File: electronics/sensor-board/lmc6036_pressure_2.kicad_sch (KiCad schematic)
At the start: 10 parts, among them U13 LMC6036, U17 LMC6036

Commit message: work on sensor-board
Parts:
- removed U13, U17: LMC6036, LMC6036:SOP65P640X120-14N, symbol LMC6036_custom:LMC6036
- added U12: LMC6036, LMC6036:SOP65P640X120-14N, symbol LMC6036_custom:LMC6036
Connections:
- net VDD: now also U12.4 (VDD)
- net VSS: now also U12.11 (VSS)
- net output_A: now also U12.1 (OUTA), U12.2 (INA-)
- net output_B: now also U12.6 (INB-), U12.7 (OUTB)
- net output_C: now also U12.8 (OUTC), U12.9 (INC-)
- net output_D: now also U12.13 (IND-), U12.14 (OUTD)
- net at R92.1, R96.1: now also U12.10 (INC+)
- net at R90.1, R94.1: now also U12.3 (INA+)
- net at R93.1, R97.1: now also U12.12 (IND+)
- net at R91.1, R95.1: now also U12.5 (INB+)
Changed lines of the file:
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@@
   (junction (at 142.24 120.65) (diameter 0) (color 0 0 0 0))
   (junction (at 142.24 148.59) (diameter 0) (color 0 0 0 0))
-  (junction (at 162.56 63.5) (diameter 0) (color 0 0 0 0))
-  (junction (at 162.56 90.17) (diameter 0) (color 0 0 0 0))
-  (junction (at 162.56 118.11) (diameter 0) (color 0 0 0 0))
-  (junction (at 162.56 146.05) (diameter 0) (color 0 0 0 0))
   (wire (pts (xy 125.73 60.96) (xy 135.89 60.96))
     (stroke (width 0) (type default) (color 0 0 0 0))
@@
   (symbol (lib_id "LMC6036_custom:LMC6036") (at 153.67 44.45 90) (unit 5)
     (in_bom yes) (on_board yes) (fields_autoplaced)
-    (property "Reference" "U13" (id 0) (at 153.67 35.56 90))
+    (property "Reference" "U12" (id 0) (at 153.67 35.56 90))
     (property "Value" "LMC6036" (id 1) (at 153.67 38.1 90))
     (property "Footprint" "LMC6036:SOP65P640X120-14N" (id 2) (at 153.67 42.545 0)
@@
   )
   (symbol (lib_id "LMC6036_custom:LMC6036") (at 153.67 63.5 0) (unit 1)
-    (in_bom yes) (on_board yes)
-    (property "Reference" "U17" (id 0) (at 154.94 53.34 0))
-    (property "Value" "LMC6036" (id 1) (at 160.02 68.58 0))
+    (in_bom yes) (on_board yes) (fields_autoplaced)
+    (property "Reference" "U12" (id 0) (at 154.94 53.34 0))
+    (property "Value" "LMC6036" (id 1) (at 154.94 55.88 0))
     (property "Footprint" "LMC6036:SOP65P640X120-14N" (id 2) (at 155.575 63.5 0)
       (effects (font (size 1.27 1.27)) hide)
@@
   (symbol (lib_id "LMC6036_custom:LMC6036") (at 153.67 90.17 0) (unit 2)
     (in_bom yes) (on_board yes) (fields_autoplaced)
-    (property "Reference" "U13" (id 0) (at 154.94 80.01 0))
+    (property "Reference" "U12" (id 0) (at 154.94 80.01 0))
     (property "Value" "LMC6036" (id 1) (at 154.94 82.55 0))
     (property "Footprint" "LMC6036:SOP65P640X120-14N" (id 2) (at 155.575 90.17 0)
@@
   (symbol (lib_id "LMC6036_custom:LMC6036") (at 153.67 118.11 0) (unit 3)
     (in_bom yes) (on_board yes) (fields_autoplaced)
-    (property "Reference" "U13" (id 0) (at 154.94 107.95 0))
+    (property "Reference" "U12" (id 0) (at 154.94 107.95 0))
     (property "Value" "LMC6036" (id 1) (at 154.94 110.49 0))
     (property "Footprint" "LMC6036:SOP65P640X120-14N" (id 2) (at 155.575 118.11 0)
@@
   (symbol (lib_id "LMC6036_custom:LMC6036") (at 153.67 146.05 0) (unit 4)
     (in_bom yes) (on_board yes) (fields_autoplaced)
-    (property "Reference" "U13" (id 0) (at 154.94 135.89 0))
+    (property "Reference" "U12" (id 0) (at 154.94 135.89 0))
     (property "Value" "LMC6036" (id 1) (at 154.94 138.43 0))
     (property "Footprint" "LMC6036:SOP65P640X120-14N" (id 2) (at 155.575 146.05 0)

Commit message: More work on sensor-board
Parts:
- R90, R91, R92, R93, R94, R95, R96, R97: value 150 -> 100
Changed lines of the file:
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@@
     (in_bom yes) (on_board yes) (fields_autoplaced)
     (property "Reference" "R92" (id 0) (at 135.89 114.3 90))
-    (property "Value" "150" (id 1) (at 135.89 116.84 90))
+    (property "Value" "100" (id 1) (at 135.89 116.84 90))
     (property "Footprint" "Resistor_SMD:R_0603_1608Metric" (id 2) (at 135.89 118.872 90)
       (effects (font (size 1.27 1.27)) hide)
@@
     (in_bom yes) (on_board yes) (fields_autoplaced)
     (property "Reference" "R93" (id 0) (at 135.89 142.24 90))
-    (property "Value" "150" (id 1) (at 135.89 144.78 90))
+    (property "Value" "100" (id 1) (at 135.89 144.78 90))
     (property "Footprint" "Resistor_SMD:R_0603_1608Metric" (id 2) (at 135.89 146.812 90)
       (effects (font (size 1.27 1.27)) hide)
@@
     (in_bom yes) (on_board yes) (fields_autoplaced)
     (property "Reference" "R90" (id 0) (at 135.89 59.69 90))
-    (property "Value" "150" (id 1) (at 135.89 62.23 90))
+    (property "Value" "100" (id 1) (at 135.89 62.23 90))
     (property "Footprint" "Resistor_SMD:R_0603_1608Metric" (id 2) (at 135.89 64.262 90)
       (effects (font (size 1.27 1.27)) hide)
@@
       (effects (font (size 1.27 1.27)) (justify left))
     )
-    (property "Value" "150" (id 1) (at 144.78 72.3899 0)
+    (property "Value" "100" (id 1) (at 144.78 72.3899 0)
       (effects (font (size 1.27 1.27)) (justify left))
     )
@@
       (effects (font (size 1.27 1.27)) (justify left))
     )
-    (property "Value" "150" (id 1) (at 144.78 99.0599 0)
+    (property "Value" "100" (id 1) (at 144.78 99.0599 0)
       (effects (font (size 1.27 1.27)) (justify left))
     )
@@
     (in_bom yes) (on_board yes) (fields_autoplaced)
     (property "Reference" "R91" (id 0) (at 135.89 86.36 90))
-    (property "Value" "150" (id 1) (at 135.89 88.9 90))
+    (property "Value" "100" (id 1) (at 135.89 88.9 90))
     (property "Footprint" "Resistor_SMD:R_0603_1608Metric" (id 2) (at 135.89 90.932 90)
       (effects (font (size 1.27 1.27)) hide)
@@
       (effects (font (size 1.27 1.27)) (justify left))
     )
-    (property "Value" "150" (id 1) (at 144.78 154.9399 0)
+    (property "Value" "100" (id 1) (at 144.78 154.9399 0)
       (effects (font (size 1.27 1.27)) (justify left))
     )
@@
       (effects (font (size 1.27 1.27)) (justify left))
     )
-    (property "Value" "150" (id 1) (at 144.78 126.9999 0)
-      (effects (font (size 1.27 1.27)) (justify left))
-    )
+    (property "Value" "100" (id 1) (at 144.78 126.9999 0)
+      (effects (font (size 1.27 1.27)) (justify left))
+    )

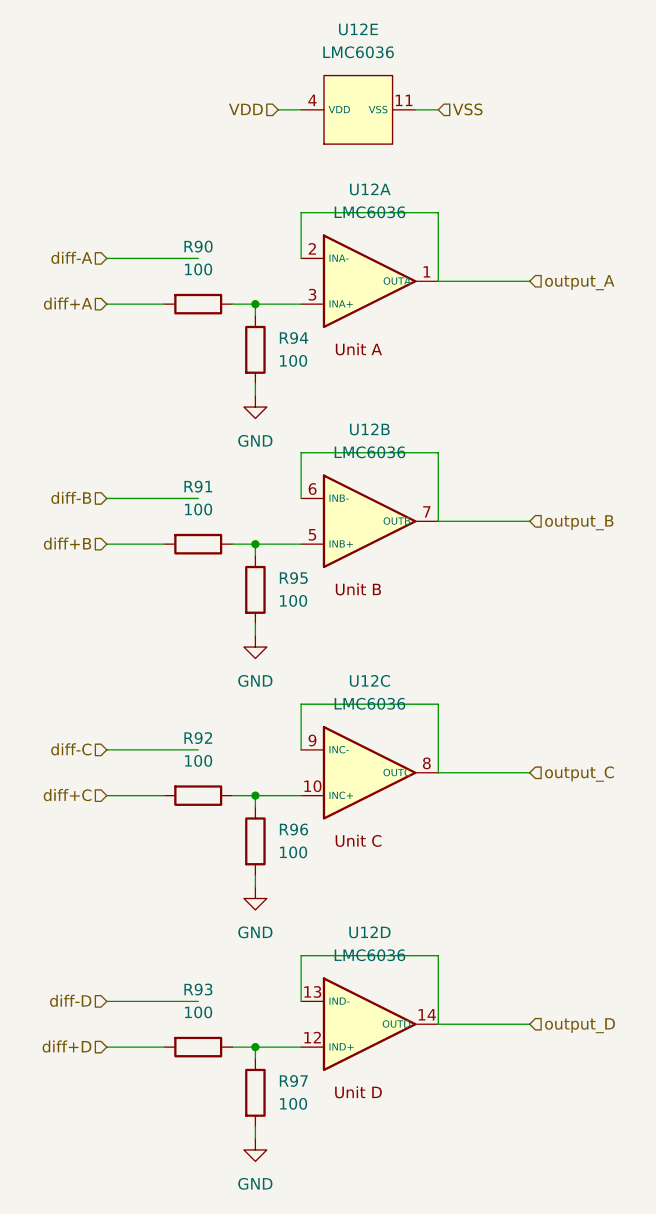
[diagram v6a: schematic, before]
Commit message: updated loadcell amplifier
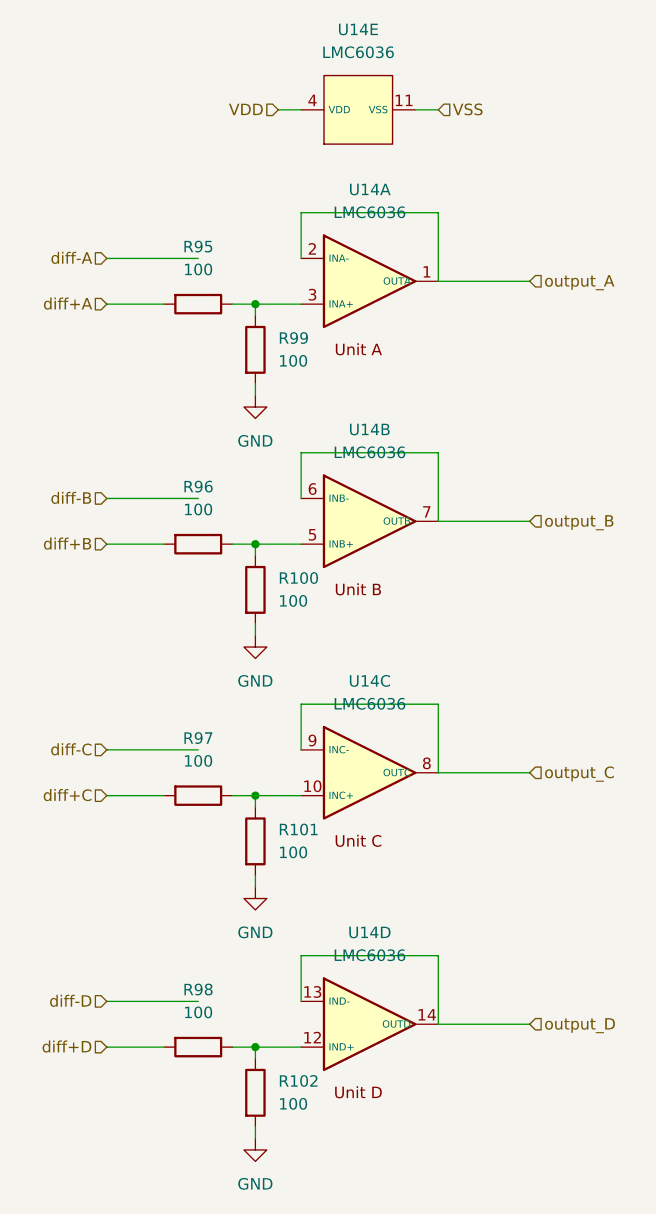
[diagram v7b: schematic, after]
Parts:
- renumbered R95 to R100, R96 to R101, R97 to R102, R90 to R95, R91 to R96, R92 to R97, R93 to R98, R94 to R99, U12 to U14
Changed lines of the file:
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@@
   (symbol (lib_id "Device:R") (at 135.89 120.65 270) (unit 1)
     (in_bom yes) (on_board yes) (fields_autoplaced)
-    (property "Reference" "R92" (id 0) (at 135.89 114.3 90))
+    (property "Reference" "R97" (id 0) (at 135.89 114.3 90))
     (property "Value" "100" (id 1) (at 135.89 116.84 90))
     (property "Footprint" "Resistor_SMD:R_0603_1608Metric" (id 2) (at 135.89 118.872 90)
@@
   (symbol (lib_id "power:GND") (at 142.24 102.87 0) (unit 1)
     (in_bom yes) (on_board yes) (fields_autoplaced)
-    (property "Reference" "#PWR0128" (id 0) (at 142.24 109.22 0)
+    (property "Reference" "#PWR0143" (id 0) (at 142.24 109.22 0)
       (effects (font (size 1.27 1.27)) hide)
     )
@@
   (symbol (lib_id "LMC6036_custom:LMC6036") (at 153.67 63.5 0) (unit 1)
     (in_bom yes) (on_board yes) (fields_autoplaced)
-    (property "Reference" "U12" (id 0) (at 154.94 53.34 0))
+    (property "Reference" "U14" (id 0) (at 154.94 53.34 0))
     (property "Value" "LMC6036" (id 1) (at 154.94 55.88 0))
     (property "Footprint" "LMC6036:SOP65P640X120-14N" (id 2) (at 155.575 63.5 0)
@@
   (symbol (lib_id "LMC6036_custom:LMC6036") (at 153.67 118.11 0) (unit 3)
     (in_bom yes) (on_board yes) (fields_autoplaced)
-    (property "Reference" "U12" (id 0) (at 154.94 107.95 0))
+    (property "Reference" "U14" (id 0) (at 154.94 107.95 0))
     (property "Value" "LMC6036" (id 1) (at 154.94 110.49 0))
     (property "Footprint" "LMC6036:SOP65P640X120-14N" (id 2) (at 155.575 118.11 0)
@@
   (symbol (lib_id "Device:R") (at 135.89 148.59 270) (unit 1)
     (in_bom yes) (on_board yes) (fields_autoplaced)
-    (property "Reference" "R93" (id 0) (at 135.89 142.24 90))
+    (property "Reference" "R98" (id 0) (at 135.89 142.24 90))
     (property "Value" "100" (id 1) (at 135.89 144.78 90))
     (property "Footprint" "Resistor_SMD:R_0603_1608Metric" (id 2) (at 135.89 146.812 90)
@@
   (symbol (lib_id "Device:R") (at 135.89 66.04 270) (unit 1)
     (in_bom yes) (on_board yes) (fields_autoplaced)
-    (property "Reference" "R90" (id 0) (at 135.89 59.69 90))
+    (property "Reference" "R95" (id 0) (at 135.89 59.69 90))
     (property "Value" "100" (id 1) (at 135.89 62.23 90))
     (property "Footprint" "Resistor_SMD:R_0603_1608Metric" (id 2) (at 135.89 64.262 90)
@@
   (symbol (lib_id "power:GND") (at 142.24 130.81 0) (unit 1)
     (in_bom yes) (on_board yes) (fields_autoplaced)
-    (property "Reference" "#PWR0129" (id 0) (at 142.24 137.16 0)
+    (property "Reference" "#PWR0144" (id 0) (at 142.24 137.16 0)
       (effects (font (size 1.27 1.27)) hide)
     )
@@
   (symbol (lib_id "LMC6036_custom:LMC6036") (at 153.67 146.05 0) (unit 4)
     (in_bom yes) (on_board yes) (fields_autoplaced)
-    (property "Reference" "U12" (id 0) (at 154.94 135.89 0))
+    (property "Reference" "U14" (id 0) (at 154.94 135.89 0))
     (property "Value" "LMC6036" (id 1) (at 154.94 138.43 0))
     (property "Footprint" "LMC6036:SOP65P640X120-14N" (id 2) (at 155.575 146.05 0)
@@
   (symbol (lib_id "Device:R") (at 142.24 71.12 0) (unit 1)
     (in_bom yes) (on_board yes) (fields_autoplaced)
-    (property "Reference" "R94" (id 0) (at 144.78 69.8499 0)
+    (property "Reference" "R99" (id 0) (at 144.78 69.8499 0)
       (effects (font (size 1.27 1.27)) (justify left))
     )
@@
   (symbol (lib_id "Device:R") (at 142.24 97.79 0) (unit 1)
     (in_bom yes) (on_board yes) (fields_autoplaced)
-    (property "Reference" "R95" (id 0) (at 144.78 96.5199 0)
+    (property "Reference" "R100" (id 0) (at 144.78 96.5199 0)
       (effects (font (size 1.27 1.27)) (justify left))
     )
@@
   (symbol (lib_id "power:GND") (at 142.24 76.2 0) (unit 1)
     (in_bom yes) (on_board yes) (fields_autoplaced)
-    (property "Reference" "#PWR0127" (id 0) (at 142.24 82.55 0)
+    (property "Reference" "#PWR0142" (id 0) (at 142.24 82.55 0)
       (effects (font (size 1.27 1.27)) hide)
     )
@@
   (symbol (lib_id "Device:R") (at 135.89 92.71 270) (unit 1)
     (in_bom yes) (on_board yes) (fields_autoplaced)
-    (property "Reference" "R91" (id 0) (at 135.89 86.36 90))
+    (property "Reference" "R96" (id 0) (at 135.89 86.36 90))
     (property "Value" "100" (id 1) (at 135.89 88.9 90))
     (property "Footprint" "Resistor_SMD:R_0603_1608Metric" (id 2) (at 135.89 90.932 90)
@@
   (symbol (lib_id "LMC6036_custom:LMC6036") (at 153.67 44.45 90) (unit 5)
     (in_bom yes) (on_board yes) (fields_autoplaced)
-    (property "Reference" "U12" (id 0) (at 153.67 35.56 90))
+    (property "Reference" "U14" (id 0) (at 153.67 35.56 90))
     (property "Value" "LMC6036" (id 1) (at 153.67 38.1 90))
     (property "Footprint" "LMC6036:SOP65P640X120-14N" (id 2) (at 153.67 42.545 0)
@@
   (symbol (lib_id "Device:R") (at 142.24 153.67 0) (unit 1)
     (in_bom yes) (on_board yes) (fields_autoplaced)
-    (property "Reference" "R97" (id 0) (at 144.78 152.3999 0)
+    (property "Reference" "R102" (id 0) (at 144.78 152.3999 0)
       (effects (font (size 1.27 1.27)) (justify left))
     )
@@
   (symbol (lib_id "power:GND") (at 142.24 158.75 0) (unit 1)
     (in_bom yes) (on_board yes) (fields_autoplaced)
-    (property "Reference" "#PWR0130" (id 0) (at 142.24 165.1 0)
+    (property "Reference" "#PWR0145" (id 0) (at 142.24 165.1 0)
       (effects (font (size 1.27 1.27)) hide)
     )
@@
   (symbol (lib_id "LMC6036_custom:LMC6036") (at 153.67 90.17 0) (unit 2)
     (in_bom yes) (on_board yes) (fields_autoplaced)
-    (property "Reference" "U12" (id 0) (at 154.94 80.01 0))
+    (property "Reference" "U14" (id 0) (at 154.94 80.01 0))
     (property "Value" "LMC6036" (id 1) (at 154.94 82.55 0))
     (property "Footprint" "LMC6036:SOP65P640X120-14N" (id 2) (at 155.575 90.17 0)
@@
   (symbol (lib_id "Device:R") (at 142.24 125.73 0) (unit 1)
     (in_bom yes) (on_board yes) (fields_autoplaced)
-    (property "Reference" "R96" (id 0) (at 144.78 124.4599 0)
-      (effects (font (size 1.27 1.27)) (justify left))
-    )
+    (property "Reference" "R101" (id 0) (at 144.78 124.4599 0)
+      (effects (font (size 1.27 1.27)) (justify left))
+    )
